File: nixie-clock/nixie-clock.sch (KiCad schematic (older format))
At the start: 30 parts

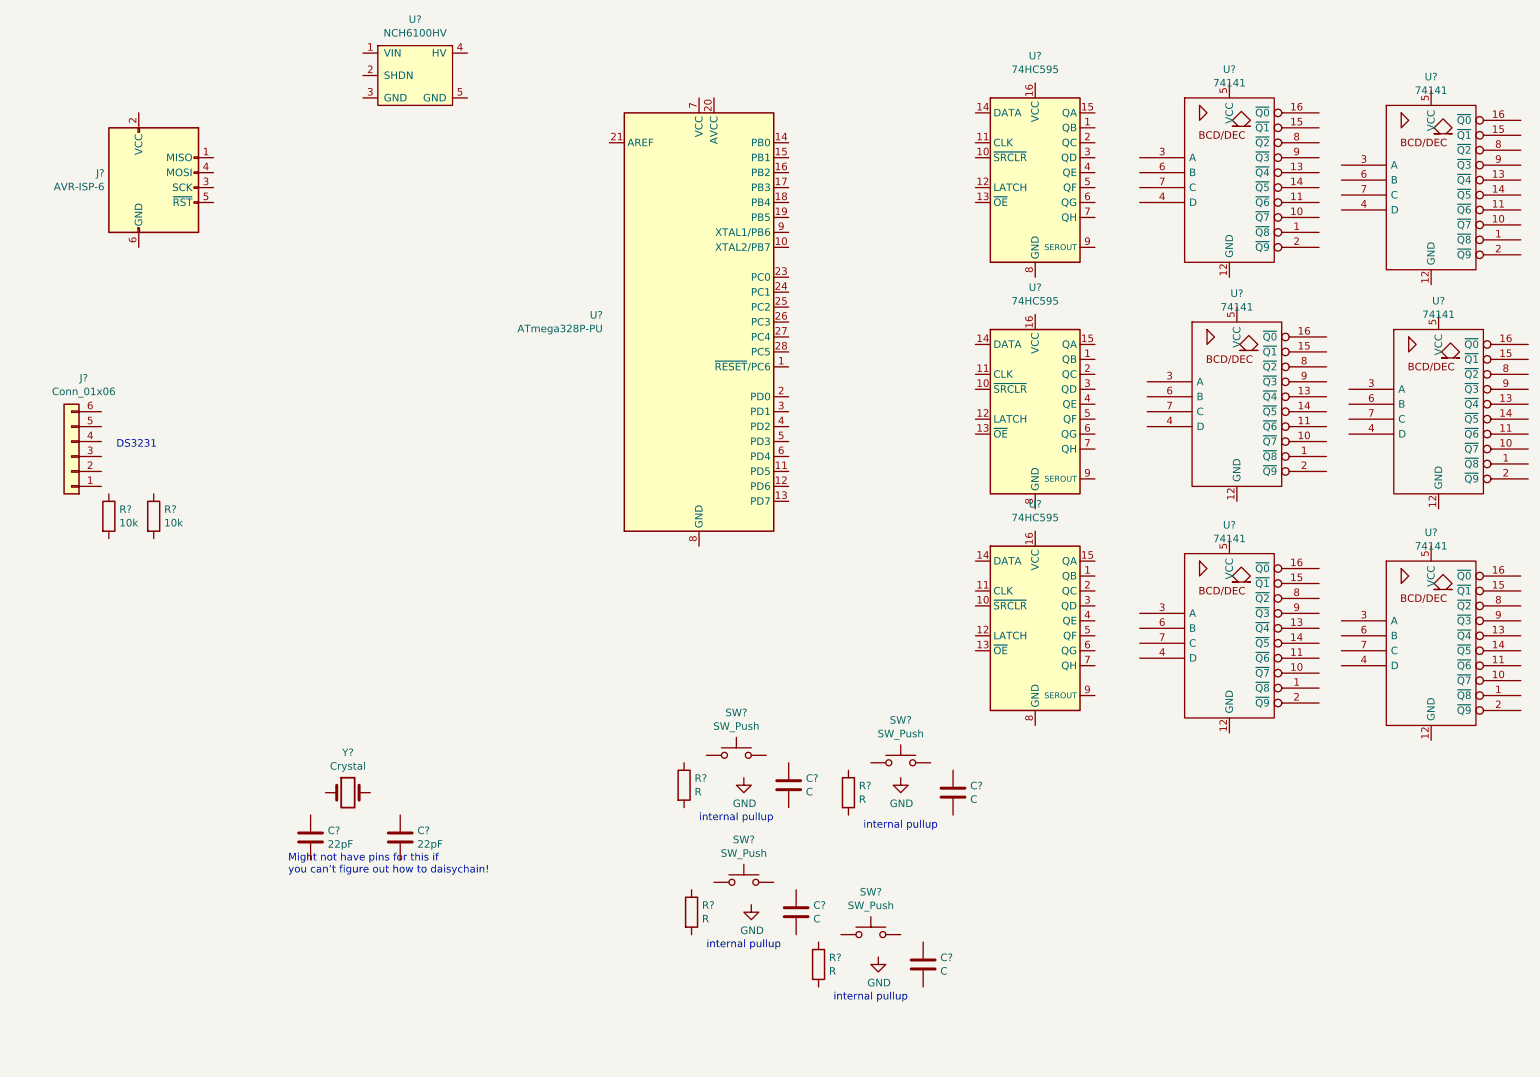
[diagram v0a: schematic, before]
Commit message: Worked on schematic. Added child sheet. See TODO at left of root. Created Mini360 symbol.
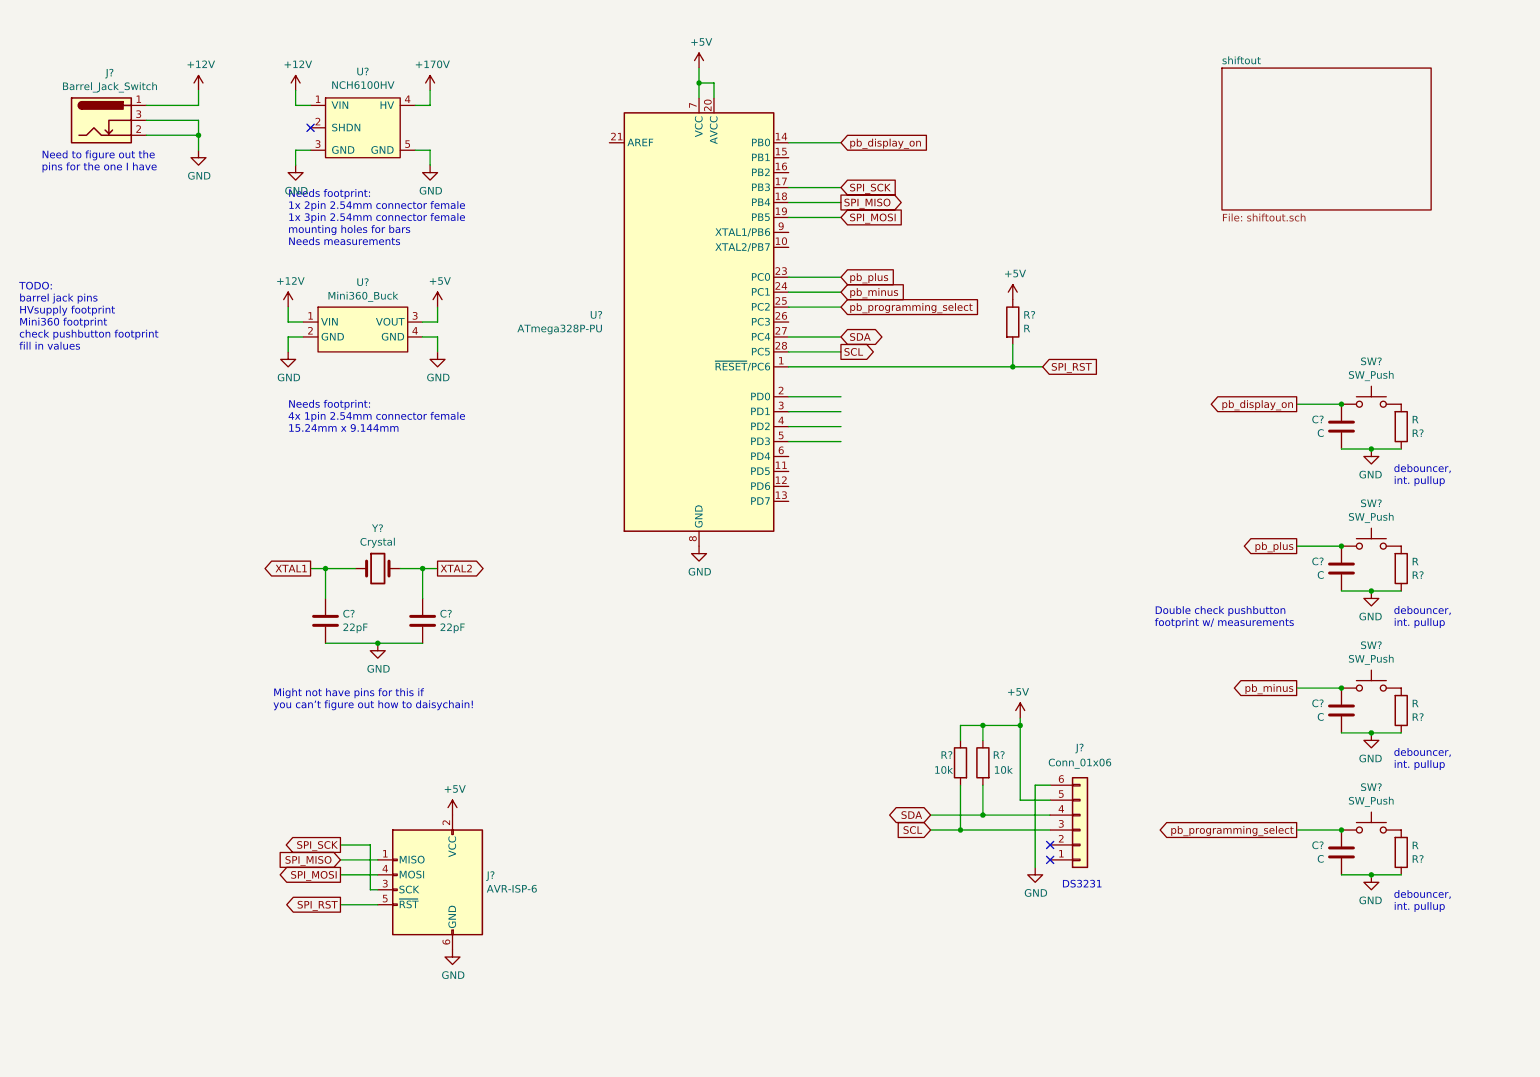
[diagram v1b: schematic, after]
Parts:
- removed C? (x4): C, symbol Device:C
- removed R? (x4): R, symbol Device:R
- removed SW? (x4): SW_Push, symbol Switch:SW_Push
- removed U? (x3): 74HC595, symbol 74xx:74HC595
- removed U? (x6): 74141, symbol 74xx_IEEE:74141
- added C? (x4): C, symbol Device:C
- added J?: Barrel_Jack_Switch, Connector_BarrelJack:BarrelJack_CUI_PJ-102AH_Horizontal, symbol Connector:Barrel_Jack_Switch
- added R? (x5): R, symbol Device:R
- added SW? (x4): SW_Push, Button_Switch_THT:SW_PUSH_6mm, symbol Switch:SW_Push
- added U?: Mini360_Buck, symbol symbols-nad:Mini360_Buck
- J?: footprint (none) -> Connector_PinSocket_2.54mm:PinSocket_1x06_P2.54mm_Vertical
- J?: footprint (none) -> Connector_PinHeader_2.54mm:PinHeader_2x03_P2.54mm_Vertical
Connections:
- net labels added: +12V, +170V, +5V, SCL, SDA, SPI_MISO, SPI_MOSI, SPI_RST, SPI_SCK, XTAL1, XTAL2, pb_display_on, pb_minus, pb_plus, pb_programming_select
- wire segments 0 -> 83
- no-connect marks 0 -> 3
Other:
- note added: "Double check pushbutton\nfootprint w/ measurements"
- note added: "Need to figure out the\npins for the one I have"
- note added: "Needs footprint:\n1x 2pin 2.54mm connector female\n1x 3pin 2.54mm connector female\nmounting holes for bars\nNeeds measurements"
- note added: "Needs footprint:\n4x 1pin 2.54mm connector female\n15.24mm x 9.144mm"
- note added: "TODO:\nbarrel jack pins\nHVsupply footprint\nMini360 footprint\ncheck pushbutton footprint\nfill in values\n"
- note added: "debouncer,\nint. pullup"
- note removed: "internal pullup"
- moved on the sheet: C?, J?, R?, U?, Y?

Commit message: Added footprint for NCH6100HV switching power supply.
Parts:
- added C?: C, symbol Device:C
- U?: footprint (none) -> footprints-nad:NCH6100HV_PinSockets
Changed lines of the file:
@@
 F 0 "U?" H 2950 1725 50  0000 C CNN
 F 1 "NCH6100HV" H 2950 1634 50  0000 C CNN
-F 2 "" H 2950 1350 50  0001 C CNN
+F 2 "footprints-nad:NCH6100HV_PinSockets" H 2950 1350 50  0001 C CNN
 F 3 "" H 2950 1350 50  0001 C CNN
 	1    2950 1350
@@
 Text Notes 650  2850 0    50   ~ 0
 TODO:\nbarrel jack pins\nHVsupply footprint\nMini360 footprint\ncheck pushbutton footprint\nfill in values\n
+$Comp
+L power:GND #PWR?
+U 1 1 5E8AC237
+P 6000 1150
+F 0 "#PWR?" H 6000 900 50  0001 C CNN
+F 1 "GND" H 6005 977 50  0000 C CNN
+F 2 "" H 6000 1150 50  0001 C CNN
+F 3 "" H 6000 1150 50  0001 C CNN
+	1    6000 1150
+	1    0    0    -1
+$EndComp
+$Comp
+L power:+5V #PWR?
+U 1 1 5E8AC419
+P 6000 850
+F 0 "#PWR?" H 6000 700 50  0001 C CNN
+F 1 "+5V" H 6015 1023 50  0000 C CNN
+F 2 "" H 6000 850 50  0001 C CNN
+F 3 "" H 6000 850 50  0001 C CNN
+	1    6000 850
+	1    0    0    -1
+$EndComp
+$Comp
+L Device:C C?
+U 1 1 5E8ACB0F
+P 6000 1000
+F 0 "C?" H 6115 1046 50  0000 L CNN
+F 1 "C" H 6115 955 50  0000 L CNN
+F 2 "" H 6038 850 50  0001 C CNN
+F 3 "~" H 6000 1000 50  0001 C CNN
+	1    6000 1000
+	-1   0    0    -1
+$EndComp
 $EndSCHEMATC

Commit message: Added footprints for mini360 buck and nichicon 1uf 250v film cap. Updated nixie-clock schematic with values. Starting to update schematic with daisy-chained configuration now that I figured out the problem with the circuit.
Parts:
- added C?: 1uF, footprints-nad:Cap_Film_250V_1uF_Nichicon, symbol Device:C
- C? (x4): value C -> 0.1uF
- R?: value R -> 10k
- R? (x4): value R -> 1k
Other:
- note added: "Lesson:\n3-2 connection breaks upon plug insertion\nCan be used in battery circuits or plugged-in\ndetection."
- note added: "TODO:\nAdd IN-3 + resistor\nfill in values\n"
- note removed: "Need to figure out the\npins for the one I have"
- note removed: "Needs footprint:\n1x 2pin 2.54mm connector female\n1x 3pin 2.54mm connector female\nmounting holes for bars\nNeeds measurements"
- note removed: "Needs footprint:\n4x 1pin 2.54mm connector female\n15.24mm x 9.144mm"
- note removed: "TODO:\nbarrel jack pins\nHVsupply footprint\nMini360 footprint\ncheck pushbutton footprint\nfill in values\n"
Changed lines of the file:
@@
 P 9500 5250
 F 0 "C?" H 9615 5296 50  0000 L CNN
-F 1 "C" H 9615 5205 50  0000 L CNN
+F 1 "0.1uF" H 9615 5205 50  0000 L CNN
 F 2 "" H 9538 5100 50  0001 C CNN
 F 3 "~" H 9500 5250 50  0001 C CNN
@@
 P 9900 5250
 F 0 "R?" H 9970 5296 50  0000 L CNN
-F 1 "R" H 9970 5205 50  0000 L CNN
+F 1 "1k" H 9970 5205 50  0000 L CNN
 F 2 "" V 9830 5250 50  0001 C CNN
 F 3 "~" H 9900 5250 50  0001 C CNN
@@
 P 9500 6200
 F 0 "C?" H 9615 6246 50  0000 L CNN
-F 1 "C" H 9615 6155 50  0000 L CNN
+F 1 "0.1uF" H 9615 6155 50  0000 L CNN
 F 2 "" H 9538 6050 50  0001 C CNN
 F 3 "~" H 9500 6200 50  0001 C CNN
@@
 P 9900 6200
 F 0 "R?" H 9970 6246 50  0000 L CNN
-F 1 "R" H 9970 6155 50  0000 L CNN
+F 1 "1k" H 9970 6155 50  0000 L CNN
 F 2 "" V 9830 6200 50  0001 C CNN
 F 3 "~" H 9900 6200 50  0001 C CNN
@@
 P 9500 3350
 F 0 "C?" H 9615 3396 50  0000 L CNN
-F 1 "C" H 9615 3305 50  0000 L CNN
+F 1 "0.1uF" H 9615 3305 50  0000 L CNN
 F 2 "" H 9538 3200 50  0001 C CNN
 F 3 "~" H 9500 3350 50  0001 C CNN
@@
 P 9900 3350
 F 0 "R?" H 9970 3396 50  0000 L CNN
-F 1 "R" H 9970 3305 50  0000 L CNN
+F 1 "1k" H 9970 3305 50  0000 L CNN
 F 2 "" V 9830 3350 50  0001 C CNN
 F 3 "~" H 9900 3350 50  0001 C CNN
@@
 P 9500 4300
 F 0 "C?" H 9615 4346 50  0000 L CNN
-F 1 "C" H 9615 4255 50  0000 L CNN
+F 1 "0.1uF" H 9615 4255 50  0000 L CNN
 F 2 "" H 9538 4150 50  0001 C CNN
 F 3 "~" H 9500 4300 50  0001 C CNN
@@
 P 9900 4300
 F 0 "R?" H 9970 4346 50  0000 L CNN
-F 1 "R" H 9970 4255 50  0000 L CNN
+F 1 "1k" H 9970 4255 50  0000 L CNN
 F 2 "" V 9830 4300 50  0001 C CNN
 F 3 "~" H 9900 4300 50  0001 C CNN
@@
 	1    0    0    -1
 $EndComp
-Text Notes 800  1650 0    50   ~ 0
-Need to figure out the\npins for the one I have
+Text Notes 600  900  0    39   ~ 0
+Lesson:\n3-2 connection breaks upon plug insertion\nCan be used in battery circuits or plugged-in\ndetection.
 Wire Wire Line
 	1500 1300 1850 1300
@@
 P 7300 2650
 F 0 "R?" H 7370 2696 50  0000 L CNN
-F 1 "R" H 7370 2605 50  0000 L CNN
+F 1 "10k" H 7370 2605 50  0000 L CNN
 F 2 "" V 7230 2650 50  0001 C CNN
 F 3 "~" H 7300 2650 50  0001 C CNN
@@
 Wire Wire Line
 	5800 3450 6150 3450
-Text Notes 2450 2150 0    50   ~ 0
-Needs footprint:\n1x 2pin 2.54mm connector female\n1x 3pin 2.54mm connector female\nmounting holes for bars\nNeeds measurements
+Wire Wire Line
+	2550 2750 2450 2750
+Wire Wire Line
+	2450 2750 2450 2850
+Wire Wire Line
+	3350 2750 3450 2750
+Wire Wire Line
+	3450 2750 3450 2850
+Wire Wire Line
+	2550 2650 2450 2650
+Wire Wire Line
+	2450 2650 2450 2550
+Wire Wire Line
+	3350 2650 3450 2650
+Wire Wire Line
+	3450 2650 3450 2550
+$Comp
+L power:GND #PWR?
+U 1 1 5E940A6F
+P 2450 2850
+F 0 "#PWR?" H 2450 2600 50  0001 C CNN
+F 1 "GND" H 2455 2677 50  0000 C CNN
+F 2 "" H 2450 2850 50  0001 C CNN
+F 3 "" H 2450 2850 50  0001 C CNN
+	1    2450 2850
+	1    0    0    -1
+$EndComp
+$Comp
+L power:GND #PWR?
+U 1 1 5E94160F
+P 3450 2850
+F 0 "#PWR?" H 3450 2600 50  0001 C CNN
+F 1 "GND" H 3455 2677 50  0000 C CNN
+F 2 "" H 3450 2850 50  0001 C CNN
+F 3 "" H 3450 2850 50  0001 C CNN
+	1    3450 2850
+	1    0    0    -1
+$EndComp
+$Comp
+L power:+12V #PWR?
+U 1 1 5E941C73
+P 2450 2550
+F 0 "#PWR?" H 2450 2400 50  0001 C CNN
+F 1 "+12V" H 2465 2723 50  0000 C CNN
+F 2 "" H 2450 2550 50  0001 C CNN
+F 3 "" H 2450 2550 50  0001 C CNN
+	1    2450 2550
+	1    0    0    -1
+$EndComp
+$Comp
+L power:+5V #PWR?
+U 1 1 5E9426F2
+P 3450 2550
+F 0 "#PWR?" H 3450 2400 50  0001 C CNN
+F 1 "+5V" H 3465 2723 50  0000 C CNN
+F 2 "" H 3450 2550 50  0001 C CNN
+F 3 "" H 3450 2550 50  0001 C CNN
+	1    3450 2550
+	1    0    0    -1
+$EndComp
+Text Notes 8250 4700 0    50   ~ 0
+Double check pushbutton\nfootprint w/ measurements
+Text Notes 650  2850 0    50   ~ 0
+TODO:\nAdd IN-3 + resistor\nfill in values\n
+$Comp
+L power:GND #PWR?
+U 1 1 5E8AC237
+P 6000 1150
+F 0 "#PWR?" H 6000 900 50  0001 C CNN
+F 1 "GND" H 6005 977 50  0000 C CNN
+F 2 "" H 6000 1150 50  0001 C CNN
+F 3 "" H 6000 1150 50  0001 C CNN
+	1    6000 1150
+	1    0    0    -1
+$EndComp
+$Comp
+L power:+5V #PWR?
+U 1 1 5E8AC419
+P 6000 850
+F 0 "#PWR?" H 6000 700 50  0001 C CNN
+F 1 "+5V" H 6015 1023 50  0000 C CNN
+F 2 "" H 6000 850 50  0001 C CNN
+F 3 "" H 6000 850 50  0001 C CNN
+	1    6000 850
+	1    0    0    -1
+$EndComp
+$Comp
+L Device:C C?
+U 1 1 5E8ACB0F
+P 6000 1000
+F 0 "C?" H 6115 1046 50  0000 L CNN
+F 1 "C" H 6115 955 50  0000 L CNN
+F 2 "" H 6038 850 50  0001 C CNN
+F 3 "~" H 6000 1000 50  0001 C CNN
+	1    6000 1000
+	-1   0    0    -1
+$EndComp
 $Comp
 L symbols-nad:Mini360_Buck U?
@@
 	1    0    0    -1
 $EndComp
-Wire Wire Line
-	2550 2750 2450 2750
-Wire Wire Line
-	2450 2750 2450 2850
-Wire Wire Line
-	3350 2750 3450 2750
-Wire Wire Line
-	3450 2750 3450 2850
-Wire Wire Line
-	2550 2650 2450 2650
-Wire Wire Line
-	2450 2650 2450 2550
-Wire Wire Line
-	3350 2650 3450 2650
-Wire Wire Line
-	3450 2650 3450 2550
-$Comp
-L power:GND #PWR?
-U 1 1 5E940A6F
-P 2450 2850
-F 0 "#PWR?" H 2450 2600 50  0001 C CNN
-F 1 "GND" H 2455 2677 50  0000 C CNN
-F 2 "" H 2450 2850 50  0001 C CNN
-F 3 "" H 2450 2850 50  0001 C CNN
-	1    2450 2850
-	1    0    0    -1
-$EndComp
-$Comp
-L power:GND #PWR?
-U 1 1 5E94160F
-P 3450 2850
-F 0 "#PWR?" H 3450 2600 50  0001 C CNN
-F 1 "GND" H 3455 2677 50  0000 C CNN
-F 2 "" H 3450 2850 50  0001 C CNN
-F 3 "" H 3450 2850 50  0001 C CNN
-	1    3450 2850
-	1    0    0    -1
-$EndComp
-$Comp
-L power:+12V #PWR?
-U 1 1 5E941C73
-P 2450 2550
-F 0 "#PWR?" H 2450 2400 50  0001 C CNN
-F 1 "+12V" H 2465 2723 50  0000 C CNN
-F 2 "" H 2450 2550 50  0001 C CNN
-F 3 "" H 2450 2550 50  0001 C CNN
-	1    2450 2550
-	1    0    0    -1
-$EndComp
-$Comp
-L power:+5V #PWR?
-U 1 1 5E9426F2
-P 3450 2550
-F 0 "#PWR?" H 3450 2400 50  0001 C CNN
-F 1 "+5V" H 3465 2723 50  0000 C CNN
-F 2 "" H 3450 2550 50  0001 C CNN
-F 3 "" H 3450 2550 50  0001 C CNN
-	1    3450 2550
-	1    0    0    -1
-$EndComp
-Text Notes 2450 3400 0    50   ~ 0
-Needs footprint:\n4x 1pin 2.54mm connector female\n15.24mm x 9.144mm
-Text Notes 8250 4700 0    50   ~ 0
-Double check pushbutton\nfootprint w/ measurements
-Text Notes 650  2850 0    50   ~ 0
-TODO:\nbarrel jack pins\nHVsupply footprint\nMini360 footprint\ncheck pushbutton footprint\nfill in values\n
-$Comp
-L power:GND #PWR?
-U 1 1 5E8AC237
-P 6000 1150
-F 0 "#PWR?" H 6000 900 50  0001 C CNN
-F 1 "GND" H 6005 977 50  0000 C CNN
-F 2 "" H 6000 1150 50  0001 C CNN
-F 3 "" H 6000 1150 50  0001 C CNN
-	1    6000 1150
-	1    0    0    -1
-$EndComp
-$Comp
-L power:+5V #PWR?
-U 1 1 5E8AC419
-P 6000 850
-F 0 "#PWR?" H 6000 700 50  0001 C CNN
-F 1 "+5V" H 6015 1023 50  0000 C CNN
-F 2 "" H 6000 850 50  0001 C CNN
-F 3 "" H 6000 850 50  0001 C CNN
-	1    6000 850
-	1    0    0    -1
-$EndComp
 $Comp
 L Device:C C?
-U 1 1 5E8ACB0F
-P 6000 1000
-F 0 "C?" H 6115 1046 50  0000 L CNN
-F 1 "C" H 6115 955 50  0000 L CNN
-F 2 "" H 6038 850 50  0001 C CNN
-F 3 "~" H 6000 1000 50  0001 C CNN
-	1    6000 1000
-	-1   0    0    -1
-$EndComp
+U 1 1 5EA13404
+P 3400 1350
+F 0 "C?" H 3515 1396 50  0000 L CNN
+F 1 "1uF" H 3515 1305 50  0000 L CNN
+F 2 "footprints-nad:Cap_Film_250V_1uF_Nichicon" H 3438 1200 50  0001 C CNN
+F 3 "~" H 3400 1350 50  0001 C CNN
+	1    3400 1350
+	1    0    0    -1
+$EndComp
+Connection ~ 3400 1200
+Connection ~ 3400 1500
 $EndSCHEMATC
